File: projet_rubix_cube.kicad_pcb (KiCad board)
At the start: 2 copper layers, 49 x 26.5 mm, 14 parts, among them J1 Screw_Terminal_01x04, J2 Screw_Terminal_01x04, J3 Screw_Terminal_01x03, U2 L298HN

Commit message: Push update schematic & PCB
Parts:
- added D14: LED_Yellow, LED_SMD:LED_0603_1608Metric, F.Cu at (173.9, 65.8)
- added D15: LED_Blue, LED_SMD:LED_0603_1608Metric, F.Cu at (171.3, 65.8)
- added D16: LED_Blue, LED_SMD:LED_0603_1608Metric, F.Cu at (168.7, 65.8)
- added D17: LED_Blue, LED_SMD:LED_0603_1608Metric, F.Cu at (166.1, 65.8)
- added D18: LED_Blue, LED_SMD:LED_0603_1608Metric, F.Cu at (163.5, 65.8)
- added D19: LED_Yellow, LED_SMD:LED_0603_1608Metric, F.Cu at (160.9, 65.8)
- added R3: 2.2K, Resistor_SMD:R_0603_1608Metric, F.Cu at (171.4, 69.8)
- added R4: 10K, Resistor_SMD:R_0603_1608Metric, F.Cu at (168.9, 69.8)
- added R5: 10K, Resistor_SMD:R_0603_1608Metric, F.Cu at (166.4, 69.8)
- added R6: 10K, Resistor_SMD:R_0603_1608Metric, F.Cu at (163.9, 69.8)
- C1: footprint Capacitor_SMD:C_0201_0603Metric -> Capacitor_SMD:C_0603_1608Metric
- C2: value 47uF -> ~; footprint Capacitor_SMD:C_0805_2012Metric -> Capacitor_SMD:C_Elec_6.3x7.7
- D1, D2, D3, D4, D5, D6, D7, D8: footprint Diode_SMD:D_SOD-323F -> Diode_SMD:D_SOD-323
- J1, J2: footprint Connector_PinHeader_1.00mm:PinHeader_1x04_P1.00mm_Horizontal -> Connector_PinHeader_1.00mm:PinHeader_1x04_P1.00mm_Vertical
- J3: footprint Connector_PinHeader_1.00mm:PinHeader_1x03_P1.00mm_Horizontal -> Connector_PinHeader_1.00mm:PinHeader_1x03_P1.00mm_Vertical
- moved J2 60.5 mm to (158.1, 68.8), turned to -90 degrees
- moved D2 58.6 mm to (170.8, 61.7), turned to -90 degrees
- moved C1 56.3 mm to (173.9, 69.8), turned to -90 degrees
- moved D1 55.3 mm to (173.7, 61.7), turned to -90 degrees
- moved D4 54.2 mm to (164.8, 61.7), turned to -90 degrees
- moved J1 51.6 mm to (158.1, 65.4), turned to -90 degrees
- moved D3 51.0 mm to (167.8, 61.7), turned to -90 degrees
- moved D7 47.8 mm to (156.0, 61.7), turned to -90 degrees
- moved D5 47.3 mm to (161.9, 61.7), turned to -90 degrees
- moved D8 46.8 mm to (153.1, 61.7), turned to -90 degrees
- moved D6 46.3 mm to (158.9, 61.7), turned to -90 degrees
- moved C2 32.3 mm to (147.5, 64.5), turned to -90 degrees
- moved U2 26.2 mm to (151.1, 39.7)
- moved J3 14.6 mm to (128.5, 40.5), turned to 0 degrees
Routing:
- net GND: track 67.5 -> 0.00 mm, vias 5 -> 0
- net +24V: track 47.8 -> 0.00 mm
- net out_bobine4: track 44.7 -> 0.00 mm, vias 1 -> 0
- net out_bobine3: track 39.0 -> 0.00 mm, vias 2 -> 0
- net out_bobine1: track 36.0 -> 0.00 mm, vias 2 -> 0
- net alim_bobine3: track 31.0 -> 0.00 mm, vias 1 -> 0
- net +5V: track 29.5 -> 0.00 mm
- net out_bobine2: track 29.0 -> 0.00 mm, vias 1 -> 0
- net alim_bobine4: track 25.9 -> 0.00 mm
- net alim_bobine2: track 20.7 -> 0.00 mm
- net alim_bobine1: track 20.2 -> 0.00 mm
- removed copper zone on F.Cu, net GND
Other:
- board outline removed

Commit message: routage_carte
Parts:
- moved D14 47.1 mm to (128.2, 54.5), turned to 180 degrees
- moved R3 43.7 mm to (131.7, 51.5), turned to 0 degrees
- moved D17 42.2 mm to (130.0, 44.0), turned to 90 degrees
- moved D18 42.1 mm to (127.5, 44.0)
- moved R6 42.0 mm to (129.0, 46.5), turned to 0 degrees
- moved R4 40.2 mm to (131.7, 54.5), turned to 0 degrees
- moved J2 39.9 mm to (125.0, 46.5), turned to 180 degrees
- moved D15 38.5 mm to (134.5, 54.5)
- moved D19 35.7 mm to (128.2, 51.5), turned to 180 degrees
- moved D1 35.2 mm to (146.0, 40.0)
- moved C1 35.1 mm to (146.0, 48.5)
- moved D3 34.5 mm to (141.0, 40.0)
- moved J1 34.3 mm to (125.0, 56.5), turned to 180 degrees
- moved D16 33.2 mm to (137.5, 54.5)
- moved R5 33.0 mm to (136.0, 57.0), turned to 0 degrees
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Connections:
- J2 pad 1: alim_bobine2 -> alim_bobine1
- J2 pad 2: alim_bobine1 -> alim_bobine2
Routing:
- net GND: track 0.00 -> 113.6 mm, vias 0 -> 2
- net +24V: track 0.00 -> 67.8 mm, vias 0 -> 4
- net +5V: track 0.00 -> 46.1 mm, vias 0 -> 1
- net out_bobine1: track 0.00 -> 44.9 mm, vias 0 -> 1
- net alim_bobine1: track 0.00 -> 44.4 mm
- net out_bobine2: track 0.00 -> 43.2 mm, vias 0 -> 1
- net alim_bobine4: track 0.00 -> 41.6 mm, vias 0 -> 1
- net out_bobine3: track 0.00 -> 40.9 mm
- net out_bobine4: track 0.00 -> 40.6 mm
- net alim_bobine3: track 0.00 -> 35.5 mm
- net alim_bobine2: track 0.00 -> 27.6 mm
- net Net-(D17-A): track 0.00 -> 7.69 mm
- net Net-(D15-A): track 0.00 -> 5.64 mm
- net Net-(D19-K): track 0.00 -> 1.89 mm
- net Net-(D14-K): track 0.00 -> 1.89 mm
- added copper zone on B.Cu, net GND
- added copper zone on F.Cu, net GND
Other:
- board outline added: 56.5 x 23.5 mm
- board text added: "5V"
- board text added: "Alime"
- board text added: "GND"
- board text added: "Phase"
- board text added: "Power good 5V"
- board text added: "Power good moteur"
- board text added: "Sortie"
- board text added: "bob1"
- board text added: "bob2"
- board text added: "bob3"
- board text added: "bob4"
- board text added: "entrées"
- board text added: "moteur"

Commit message: New rules
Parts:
- moved R4 21.6 mm to (141.0, 35.0), turned to 90 degrees
- moved D14 19.2 mm to (139.5, 39.0), turned to 90 degrees
- moved J1 15.1 mm to (133.5, 44.0), turned to 0 degrees
- moved D19 15.0 mm to (136.5, 39.0), turned to 90 degrees
- moved C1 14.7 mm to (137.5, 36.5), turned to 180 degrees
- moved C2 10.7 mm to (131.0, 37.0), turned to 0 degrees
- moved R3 10.5 mm to (134.8, 41.5), turned to 180 degrees
- moved D16 9.76 mm to (128.5, 50.7), turned to 90 degrees
- moved D5 9.30 mm to (140.5, 50.0), turned to -90 degrees
- moved J2 9.28 mm to (133.5, 50.2), turned to 0 degrees
- moved U2 9.04 mm to (143.3, 35.1)
- moved D1 8.38 mm to (138.0, 42.5)
- moved D2 8.25 mm to (138.0, 46.0)
- moved R5 7.52 mm to (129.5, 53.2), turned to 180 degrees
- moved J3 6.26 mm to (138.5, 34.5)
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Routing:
- net GND: track 113.6 -> 45.4 mm, vias 2 -> 0
- net alim_bobine1: track 44.4 -> 14.1 mm
- net alim_bobine4: track 41.6 -> 19.2 mm, vias 1 -> 0
- net out_bobine2: track 43.2 -> 26.1 mm, vias 1 -> 0
- net +24V: track 67.8 -> 52.1 mm, vias 4 -> 0
- net alim_bobine2: track 27.6 -> 13.3 mm
- net out_bobine3: track 40.9 -> 26.8 mm
- net out_bobine1: track 44.9 -> 32.4 mm, vias 1 -> 0
- net +5V: track 46.1 -> 35.1 mm, vias 1 -> 0
- net alim_bobine3: track 35.5 -> 28.1 mm
- net Net-(D17-A): track 7.69 -> 3.78 mm
- net Net-(D14-K): track 1.89 -> 4.58 mm
- net Net-(D15-A): track 5.64 -> 3.78 mm
- net out_bobine4: track 40.6 -> 39.7 mm
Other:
- board size 56.5 x 23.5 mm -> 41.5 x 26 mm
- board text added: "Q.G"
- board text removed: "5V"
- board text removed: "Alime"
- board text removed: "GND"
- board text removed: "Phase"
- board text removed: "Power good 5V"
- board text removed: "Power good moteur"
- board text removed: "Sortie"
- board text removed: "bob1"
- board text removed: "bob2"
- board text removed: "bob3"
- board text removed: "bob4"
- board text removed: "entrées"
- board text removed: "moteur"

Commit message: DRC OK
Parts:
- added ?: , , F.Cu at (124.0, 44.0)
- J1, J2: footprint Connector_PinHeader_1.00mm:PinHeader_1x04_P1.00mm_Vertical -> Connector_PinHeader_2.54mm:PinHeader_1x04_P2.54mm_Vertical
- J3: footprint Connector_PinHeader_1.00mm:PinHeader_1x03_P1.00mm_Vertical -> Connector_PinSocket_2.54mm:PinSocket_1x03_P2.54mm_Vertical
- moved C2 16.0 mm to (125.5, 52.0), turned to -90 degrees
- moved J3 15.3 mm to (124.0, 39.5), turned to 180 degrees
- moved R6 14.8 mm to (136.5, 34.0), turned to -90 degrees
- moved D17 14.5 mm to (140.5, 34.0)
- moved D18 14.5 mm to (138.5, 34.0)
- moved C1 14.4 mm to (124.0, 31.5)
- moved R4 12.6 mm to (129.0, 38.7), turned to -90 degrees
- moved D16 12.4 mm to (140.5, 53.8), turned to -90 degrees
- moved D14 11.1 mm to (129.0, 35.5)
- moved D19 10.1 mm to (127.0, 35.5)
- moved J1 9.82 mm to (133.0, 34.2)
- moved D15 8.57 mm to (138.5, 53.8), turned to 90 degrees
- moved R3 8.32 mm to (127.0, 38.7), turned to -90 degrees
- moved R5 7.02 mm to (136.5, 53.8), turned to -90 degrees
- moved D1 4.50 mm to (138.0, 38.0)
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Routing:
- net GND: track 45.4 -> 11.1 mm
- net out_bobine3: track 26.8 -> 49.9 mm
- net +24V: track 52.1 -> 72.9 mm
- net out_bobine4: track 39.7 -> 59.3 mm
- net +5V: track 35.1 -> 50.8 mm
- net out_bobine2: track 26.1 -> 19.8 mm
- net alim_bobine3: track 28.1 -> 34.1 mm
- net out_bobine1: track 32.4 -> 27.2 mm
- net alim_bobine4: track 19.2 -> 23.7 mm
- net Net-(D14-K): track 4.58 -> 1.56 mm
- net alim_bobine1: track 14.1 -> 12.7 mm
- net Net-(D17-A): track 3.78 -> 4.67 mm
- net alim_bobine2: track 13.3 -> 12.7 mm
- net Net-(D19-K): track 2.06 -> 1.56 mm
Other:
- board size 41.5 x 26 mm -> 47 x 28.5 mm
- board text added: "+5V"
- board text added: "+MOT"
- board text added: "/A"
- board text added: "/B"
- board text added: "1"
- board text added: "2"
- board text added: "3"
- board text added: "4"
- board text added: "5V MOT"
- board text added: "A"
- board text added: "B"
- board text added: "GND"
- board text added: "INPUT"
- board text added: "OUTPUT"
- board text added: "POWER"

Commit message: Modif update
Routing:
- net +5V: track 50.8 -> 51.6 mm
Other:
- board size 47 x 28.5 mm -> 47.5 x 30 mm
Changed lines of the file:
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@@
 			(outputformat 1)
 			(mirror no)
-			(drillshape 1)
+			(drillshape 0)
 			(scaleselection 1)
-			(outputdirectory "")
+			(outputdirectory "Fichier de fab/")
 		)
 	)
@@
 	)
 	(gr_rect
-		(start 120.5 30)
-		(end 167.5 58.5)
+		(start 120 29.5)
+		(end 167.5 59.5)
 		(stroke
 			(width 0.05)
@@
 		(start 143.28 45.265)
 		(end 146.735 45.265)
-		(width 0.5)
+		(width 0.3)
 		(layer "B.Cu")
 		(net 1)
 	)
 	(segment
-		(start 126.42 32)
-		(end 145 32)
+		(start 144 31)
+		(end 148 35)
 		(width 0.5)
 		(layer "B.Cu")
@@
 	)
 	(segment
-		(start 145 32)
-		(end 148 35)
+		(start 148 39.275)
+		(end 145.82 41.455)
 		(width 0.5)
 		(layer "B.Cu")
@@
 	)
 	(segment
-		(start 148 39.275)
-		(end 145.82 41.455)
+		(start 148 35)
+		(end 148 39.275)
 		(width 0.5)
 		(layer "B.Cu")
@@
 	)
 	(segment
-		(start 124 34.42)
-		(end 126.42 32)
+		(start 147.5 43.135)
+		(end 145.82 41.455)
 		(width 0.5)
 		(layer "B.Cu")
@@
 	)
 	(segment
-		(start 147.5 43.135)
-		(end 145.82 41.455)
+		(start 124 34.42)
+		(end 127.42 31)
 		(width 0.5)
 		(layer "B.Cu")
@@
 	)
 	(segment
-		(start 148 35)
-		(end 148 39.275)
+		(start 127.42 31)
+		(end 144 31)
 		(width 0.5)
 		(layer "B.Cu")
@@
 		(polygon
 			(pts
-				(xy 120.5 30) (xy 167.5 30) (xy 167.5 58.5) (xy 120.5 58.5)
+				(xy 120 29.5) (xy 167.5 29.5) (xy 167.5 59.5) (xy 120 59.5)
 			)
 		)
@@
 		(polygon
 			(pts
-				(xy 120.5 30) (xy 167.5 30) (xy 167.5 58.5) (xy 120.5 58.5)
+				(xy 120 29.5) (xy 167.5 29.5) (xy 167.5 59.5) (xy 120 59.5)
 			)
 		)

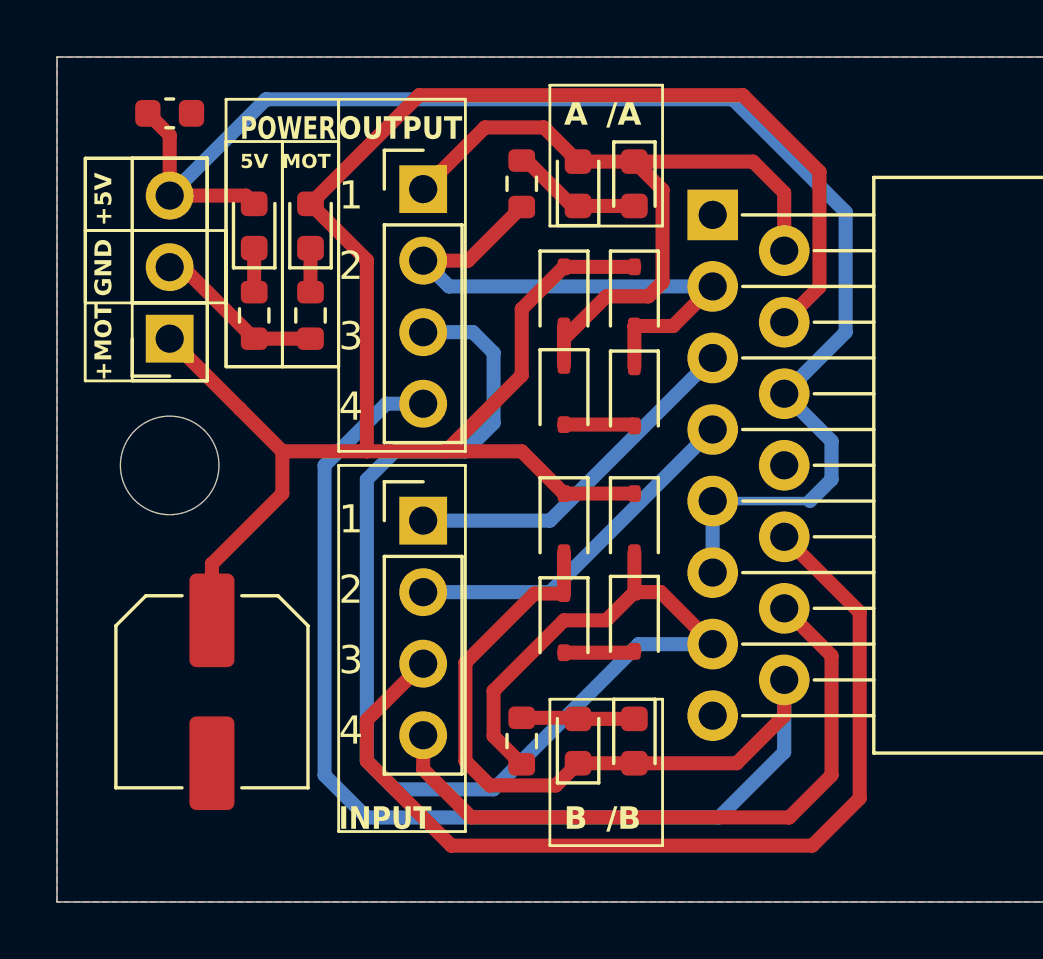
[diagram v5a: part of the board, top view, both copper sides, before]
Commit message: DRC no tracks conflit
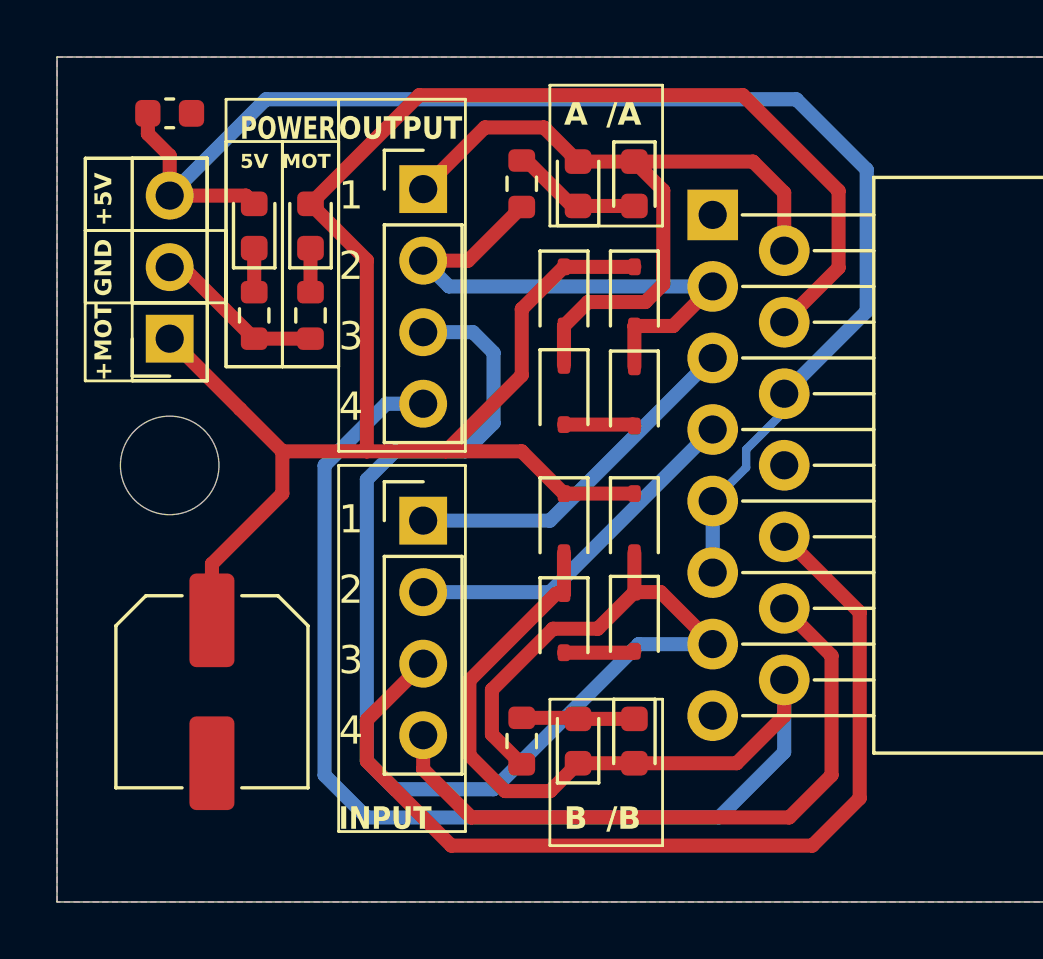
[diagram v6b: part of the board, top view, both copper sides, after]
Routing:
- net +5V: track 51.6 -> 50.1 mm
- net out_bobine4: track 59.3 -> 58.7 mm
- net +24V: track 72.9 -> 73.4 mm

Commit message: Test push
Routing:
- net alim_bobine3: track 34.1 -> 34.7 mm
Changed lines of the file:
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@@
+	)
+	(segment
+		(start 131 54.5)
+		(end 134 57.5)
+		(width 0.5)
+		(layer "F.Cu")
+		(net 4)
 	)
 	(segment
@@
 	)
 	(segment
-		(start 131 54.5)
-		(end 134 57.5)
+		(start 149.25 55.068309)
+		(end 149.25 49.965)
 		(width 0.5)
 		(layer "F.Cu")
@@
 	)
 	(segment
-		(start 148.5 55.818309)
-		(end 148.5 49.215)
+		(start 149.25 49.965)
+		(end 145.82 46.535)
 		(width 0.5)
 		(layer "F.Cu")
@@
 	)
 	(segment
-		(start 148.5 49.215)
-		(end 145.82 46.535)
+		(start 133 51.04)
+		(end 131 53.04)
 		(width 0.5)
 		(layer "F.Cu")
@@
 	)
 	(segment
-		(start 133 51.04)
-		(end 131 53.04)
+		(start 146.818309 57.5)
+		(end 149.25 55.068309)
 		(width 0.5)
 		(layer "F.Cu")
-		(net 4)
-	)
-	(segment
-		(start 146.818309 57.5)
-		(end 148.5 55.818309)
-		(width 0.5)
-		(layer "F.Cu")
